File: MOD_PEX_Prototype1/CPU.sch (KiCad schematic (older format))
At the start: 16 parts, among them P2 HEADER_5X2, P3 HEADER_5X2, U1 LPC111X_LQFP48, X1 10MHz

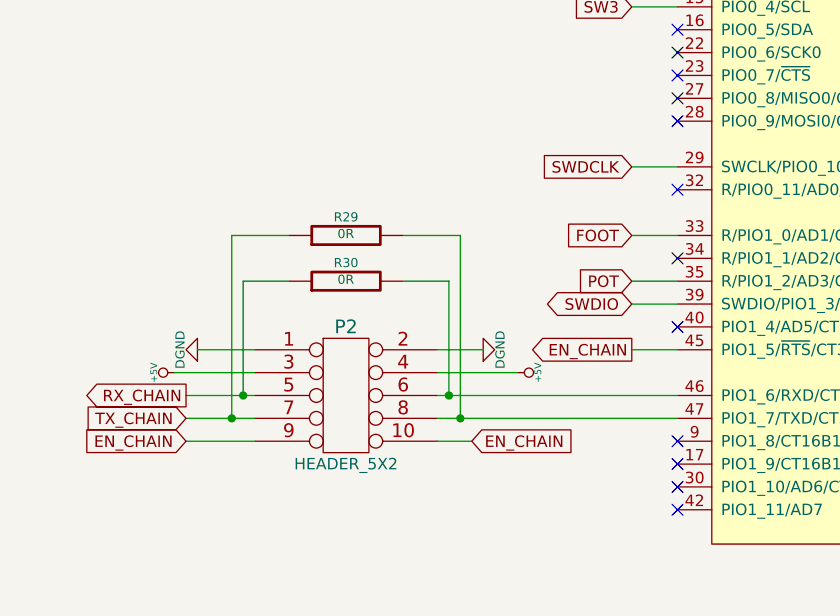
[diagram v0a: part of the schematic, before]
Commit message: Fixing control chain signal names, adding a 0R resistor for the ENABLE_CHAIN signal in the P1 debugging connector and regenerating the netlist.
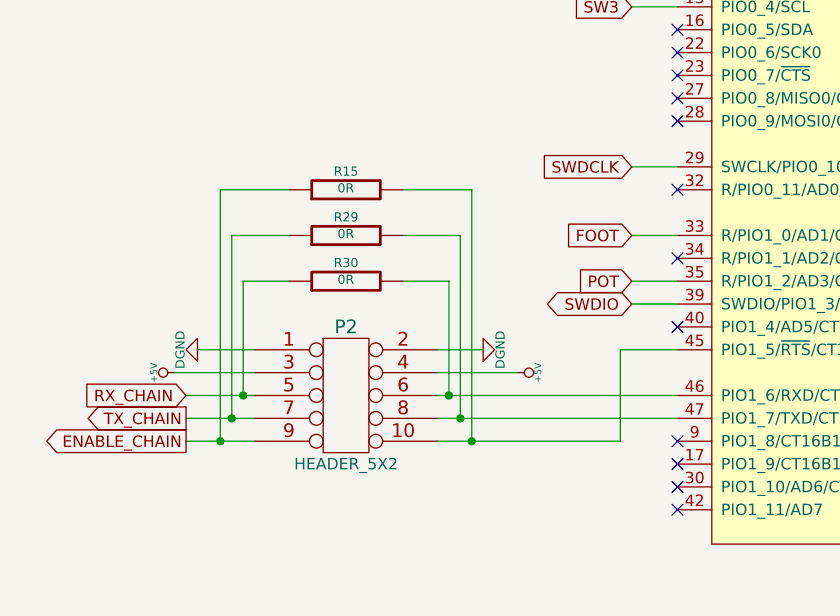
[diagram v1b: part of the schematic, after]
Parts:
- added R15: 0R, MOD_Footprints_Lib:SM0805, symbol R
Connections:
- net EN_CHAIN: no longer names the net of P2.10, U1.45 (PIO1_5/~RTS~/CT32B0_CAP0)
- net EN_CHAIN: now also R15.2; no longer P2.9
- new net ENABLE_CHAIN: P2.9, R15.1
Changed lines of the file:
@@
 $EndComp
 $Comp
-L DGND #PWR54
+L DGND #PWR048
 U 1 1 548B6D7E
 P 7050 4450
-F 0 "#PWR54" H 7050 4450 40  0001 C CNN
+F 0 "#PWR048" H 7050 4450 40  0001 C CNN
 F 1 "DGND" H 7050 4380 40  0000 C CNN
 F 2 "" H 7050 4450 60  0000 C CNN
@@
 $EndComp
 $Comp
-L DGND #PWR59
+L DGND #PWR049
 U 1 1 548B6D8B
 P 8050 4050
-F 0 "#PWR59" H 8050 4050 40  0001 C CNN
+F 0 "#PWR049" H 8050 4050 40  0001 C CNN
 F 1 "DGND" H 8050 3980 40  0000 C CNN
 F 2 "" H 8050 4050 60  0000 C CNN
@@
 $EndComp
 $Comp
-L DGND #PWR58
+L DGND #PWR050
 U 1 1 548B6D91
 P 8050 3850
-F 0 "#PWR58" H 8050 3850 40  0001 C CNN
+F 0 "#PWR050" H 8050 3850 40  0001 C CNN
 F 1 "DGND" H 8050 3780 40  0000 C CNN
 F 2 "" H 8050 3850 60  0000 C CNN
@@
 $EndComp
 $Comp
-L +3.3V #PWR55
+L +3.3V #PWR051
 U 1 1 548B6D97
 P 7450 3800
-F 0 "#PWR55" H 7450 3760 30  0001 C CNN
+F 0 "#PWR051" H 7450 3760 30  0001 C CNN
 F 1 "+3.3V" H 7450 3910 30  0000 C CNN
 F 2 "" H 7450 3800 60  0000 C CNN
@@
 $EndComp
 $Comp
-L DGND #PWR57
+L DGND #PWR052
 U 1 1 548B6DAB
 P 7850 5250
-F 0 "#PWR57" H 7850 5250 40  0001 C CNN
+F 0 "#PWR052" H 7850 5250 40  0001 C CNN
 F 1 "DGND" H 7850 5180 40  0000 C CNN
 F 2 "" H 7850 5250 60  0000 C CNN
@@
 $EndComp
 $Comp
-L DGND #PWR56
+L DGND #PWR053
 U 1 1 548B6DB1
 P 7850 4550
-F 0 "#PWR56" H 7850 4550 40  0001 C CNN
+F 0 "#PWR053" H 7850 4550 40  0001 C CNN
 F 1 "DGND" H 7850 4480 40  0000 C CNN
 F 2 "" H 7850 4550 60  0000 C CNN
@@
 $EndComp
 $Comp
-L DGND #PWR49
+L DGND #PWR054
 U 1 1 548B6DCC
 P 3650 1850
-F 0 "#PWR49" H 3650 1850 40  0001 C CNN
+F 0 "#PWR054" H 3650 1850 40  0001 C CNN
 F 1 "DGND" H 3650 1780 40  0000 C CNN
 F 2 "" H 3650 1850 60  0000 C CNN
@@
 $EndComp
 $Comp
-L +3.3V #PWR51
+L +3.3V #PWR055
 U 1 1 548B6DD2
 P 4250 1250
-F 0 "#PWR51" H 4250 1210 30  0001 C CNN
+F 0 "#PWR055" H 4250 1210 30  0001 C CNN
 F 1 "+3.3V" H 4250 1360 30  0000 C CNN
 F 2 "" H 4250 1250 60  0000 C CNN
@@
 SWDCLK
 $Comp
-L DGND #PWR53
+L DGND #PWR056
 U 1 1 548B6DE3
 P 5900 6350
-F 0 "#PWR53" H 5900 6350 40  0001 C CNN
+F 0 "#PWR056" H 5900 6350 40  0001 C CNN
 F 1 "DGND" H 5900 6280 40  0000 C CNN
 F 2 "" H 5900 6350 60  0000 C CNN
@@
 NoConn ~ 6800 6050
 NoConn ~ 6800 6150
-Text GLabel 4150 3900 0    50   Output ~ 0
-EN_CHAIN
 Text GLabel 7150 3550 2    50   Output ~ 0
 LED1
 NoConn ~ 6950 3650
 NoConn ~ 6950 3750
-Text GLabel 2200 4100 0    50   Output ~ 0
+Text GLabel 2200 4100 0    50   Input ~ 0
 RX_CHAIN
-Text GLabel 2200 4200 0    50   Input ~ 0
+Text GLabel 2200 4200 0    50   Output ~ 0
 TX_CHAIN
 $Comp
-L +5V #PWR45
+L +5V #PWR057
 U 1 1 548B6DF3
 P 2150 4000
-F 0 "#PWR45" H 2150 4090 20  0001 C CNN
+F 0 "#PWR057" H 2150 4090 20  0001 C CNN
 F 1 "+5V" H 2150 4090 30  0000 C CNN
 F 2 "" H 2150 4000 60  0000 C CNN
@@
 $EndComp
 $Comp
-L DGND #PWR46
+L DGND #PWR058
 U 1 1 548B6DF9
 P 2250 3900
-F 0 "#PWR46" H 2250 3900 40  0001 C CNN
+F 0 "#PWR058" H 2250 3900 40  0001 C CNN
 F 1 "DGND" H 2250 3825 40  0000 C CNN
 F 2 "" H 2250 3900 60  0000 C CNN
@@
 $EndComp
 $Comp
-L +3.3V #PWR47
+L +3.3V #PWR059
 U 1 1 548B6E06
 P 3300 2100
-F 0 "#PWR47" H 3300 2060 30  0001 C CNN
+F 0 "#PWR059" H 3300 2060 30  0001 C CNN
 F 1 "+3.3V" H 3300 2210 30  0000 C CNN
 F 2 "" H 3300 2100 60  0000 C CNN
@@
 	3300 4200 4350 4200
 Wire Wire Line
-	4150 3900 4350 3900
+	4100 3900 4350 3900
 Wire Wire Line
 	2200 4200 2500 4200
@@
 	6000 5850 5950 5850
 $Comp
-L +3.3V #PWR52
+L +3.3V #PWR060
 U 1 1 548B6E58
 P 5400 5850
-F 0 "#PWR52" H 5400 5810 30  0001 C CNN
+F 0 "#PWR060" H 5400 5810 30  0001 C CNN
 F 1 "+3.3V" H 5400 5960 30  0000 C CNN
 F 2 "" H 5400 5850 60  0000 C CNN
@@
 NoConn ~ 4350 4500
 NoConn ~ 4350 4600
-Text GLabel 2200 4300 0    50   Input ~ 0
-EN_CHAIN
+Text GLabel 2200 4300 0    50   Output ~ 0
+ENABLE_CHAIN
 Wire Wire Line
 	2200 4300 2500 4300
@@
 $EndComp
 $Comp
-L DGND #PWR48
+L DGND #PWR061
 U 1 1 548B6E8F
 P 3500 3900
-F 0 "#PWR48" H 3500 3900 40  0001 C CNN
+F 0 "#PWR061" H 3500 3900 40  0001 C CNN
 F 1 "DGND" H 3500 3825 40  0000 C CNN
 F 2 "" H 3500 3900 60  0000 C CNN
@@
 $EndComp
 $Comp
-L +5V #PWR50
+L +5V #PWR062
 U 1 1 548B6E95
 P 3650 4000
-F 0 "#PWR50" H 3650 4090 20  0001 C CNN
+F 0 "#PWR062" H 3650 4090 20  0001 C CNN
 F 1 "+5V" H 3650 4090 30  0000 C CNN
 F 2 "" H 3650 4000 60  0000 C CNN
@@
 	3650 4000 3300 4000
 Wire Wire Line
-	3300 4300 3450 4300
+	3300 4300 4100 4300
 $Comp
 L R R30
@@
 	0    -1   -1   0
 $EndComp
-Text GLabel 3450 4300 2    50   Input ~ 0
-EN_CHAIN
 Wire Wire Line
 	3150 3600 3350 3600
@@
 	2400 3400 2400 4200
 Connection ~ 2400 4200
+Wire Wire Line
+	4100 4300 4100 3900
+$Comp
+L R R15
+U 1 1 548F0B2A
+P 2900 3200
+F 0 "R15" V 2980 3200 40  0000 C CNN
+F 1 "0R" V 2907 3201 40  0000 C CNN
+F 2 "MOD_Footprints_Lib:SM0805" V 2830 3200 30  0001 C CNN
+F 3 "~" H 2900 3200 30  0000 C CNN
+	1    2900 3200
+	0    -1   -1   0
+$EndComp
+Wire Wire Line
+	3150 3200 3450 3200
+Wire Wire Line
+	3450 3200 3450 4300
+Connection ~ 3450 4300
+Wire Wire Line
+	2650 3200 2350 3200
+Wire Wire Line
+	2350 3200 2350 4300
+Connection ~ 2350 4300
 $EndSCHEMATC

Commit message: fix issue #11 (new control chain circuitry): tracing the PCB to incorporate schematics changes.
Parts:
- R15, R22, R29, R30: footprint MOD_Footprints_Lib:SM0805 -> MOD_Footprints_Lib:SM0603
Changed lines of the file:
@@
 F 0 "R22" V 5780 5850 40  0000 C CNN
 F 1 "0R" V 5707 5851 40  0000 C CNN
-F 2 "MOD_Footprints_Lib:SM0805" V 5630 5850 30  0001 C CNN
+F 2 "MOD_Footprints_Lib:SM0603" V 5630 5850 30  0001 C CNN
 F 3 "~" H 5700 5850 30  0000 C CNN
 	1    5700 5850
@@
 F 0 "R30" V 2980 3600 40  0000 C CNN
 F 1 "0R" V 2907 3601 40  0000 C CNN
-F 2 "MOD_Footprints_Lib:SM0805" V 2830 3600 30  0001 C CNN
+F 2 "MOD_Footprints_Lib:SM0603" V 2830 3600 30  0001 C CNN
 F 3 "~" H 2900 3600 30  0000 C CNN
 	1    2900 3600
@@
 F 0 "R29" V 2980 3400 40  0000 C CNN
 F 1 "0R" V 2907 3401 40  0000 C CNN
-F 2 "MOD_Footprints_Lib:SM0805" V 2830 3400 30  0001 C CNN
+F 2 "MOD_Footprints_Lib:SM0603" V 2830 3400 30  0001 C CNN
 F 3 "~" H 2900 3400 30  0000 C CNN
 	1    2900 3400
@@
 F 0 "R15" V 2980 3200 40  0000 C CNN
 F 1 "0R" V 2907 3201 40  0000 C CNN
-F 2 "MOD_Footprints_Lib:SM0805" V 2830 3200 30  0001 C CNN
+F 2 "MOD_Footprints_Lib:SM0603" V 2830 3200 30  0001 C CNN
 F 3 "~" H 2900 3200 30  0000 C CNN
 	1    2900 3200
